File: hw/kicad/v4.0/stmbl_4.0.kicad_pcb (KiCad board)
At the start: 2 copper layers, 100 x 100 mm, 433 parts, among them J1 RJ45_LED, J2 RJ45_LED, J3 RJ45_LED, P1 USB_OTG, P10 CONN_02X06, P11 USB_OTG, P12 CONN_01X04, P13 CONN_01X04, P14 CONN_01X04, P15 CONN_01X02, P2 CONN_01X02, P3 CONN_01X02, P4 CONN_01X02, P5 CONN_01X06, P6 CONN_01X02, P7 CONN_01X04, P8 CONN_01X03, P9 CONN_01X06, Q1 IRLML6344, Q2 IRLML6344, Q3 IRLML6344, Q4 IRLML6344, Q5 IRLML6344, T1 testpoint, T2 testpoint, T44 testpoint, T45 testpoint, T46 testpoint, U1 USBLC6-4SC6, U10 SN65176B, U11 SN65176B, U12 IRAM256a, U13 ACT4088, U14 SN65176B, U15 SN65176B, U16 SN65176B, U17 SN65176B, U18 SN65176B, U19 SN65176B, U2 zldo1117, U20 USBLC6-4SC6, U21 USBLC6-4SC6, U22 USBLC6-4SC6, U23 USBLC6-4SC6, U24 non_plated, U25 STM32F303CBTx, U26 STM32F405VG, U27 ACT4088, U28 ACT4088, U29 USBLC6-4SC6, U3 SI8621, U30 non_plated, U31 non_plated, U32 non_plated, U33 heatsink, U34 fan, U35 non_plated, U36 non_plated, U37 non_plated, U39 non_plated, U4 ACT4088, U5 LNK304D, U6 LM358, U7 LM358, U8 SN65176B, U9 SN65176B, Y1 8M, Y2 8M

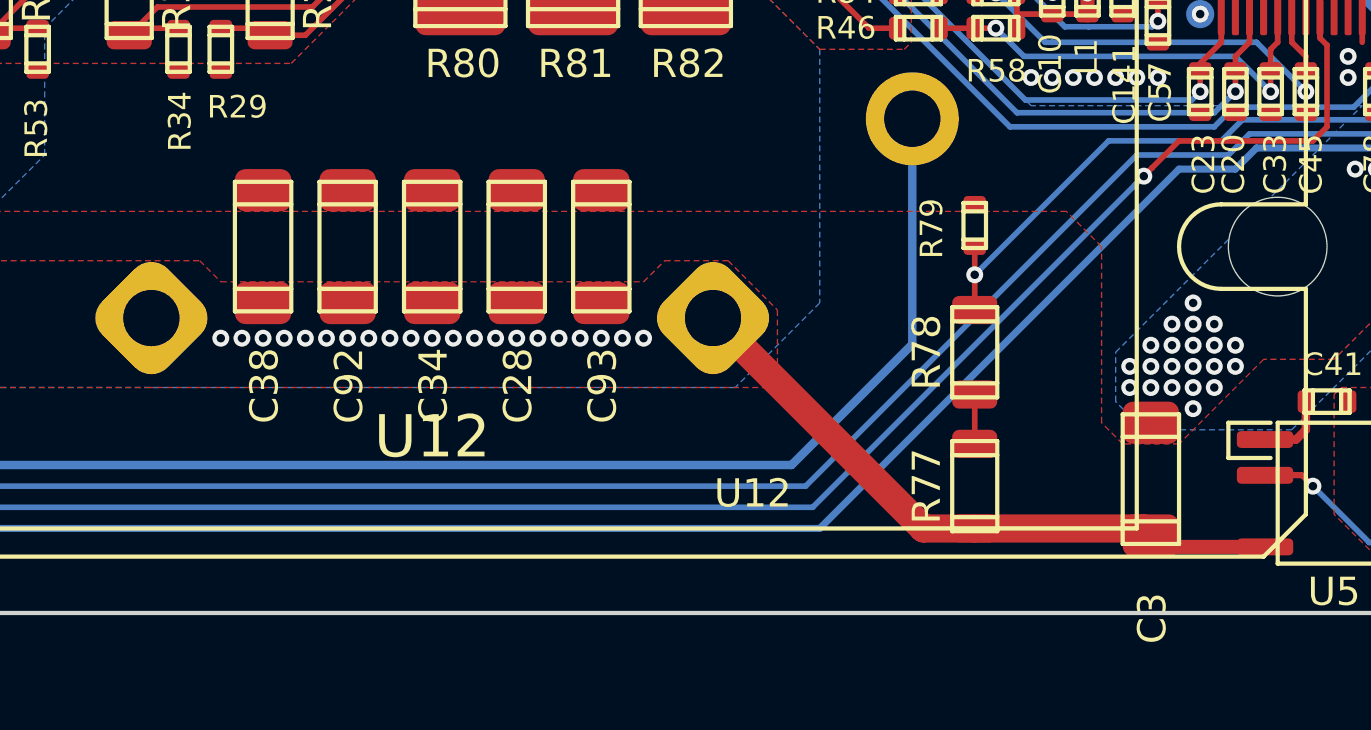
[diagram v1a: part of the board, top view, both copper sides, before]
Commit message: Changed 120uf 1808 to 1210 100uF
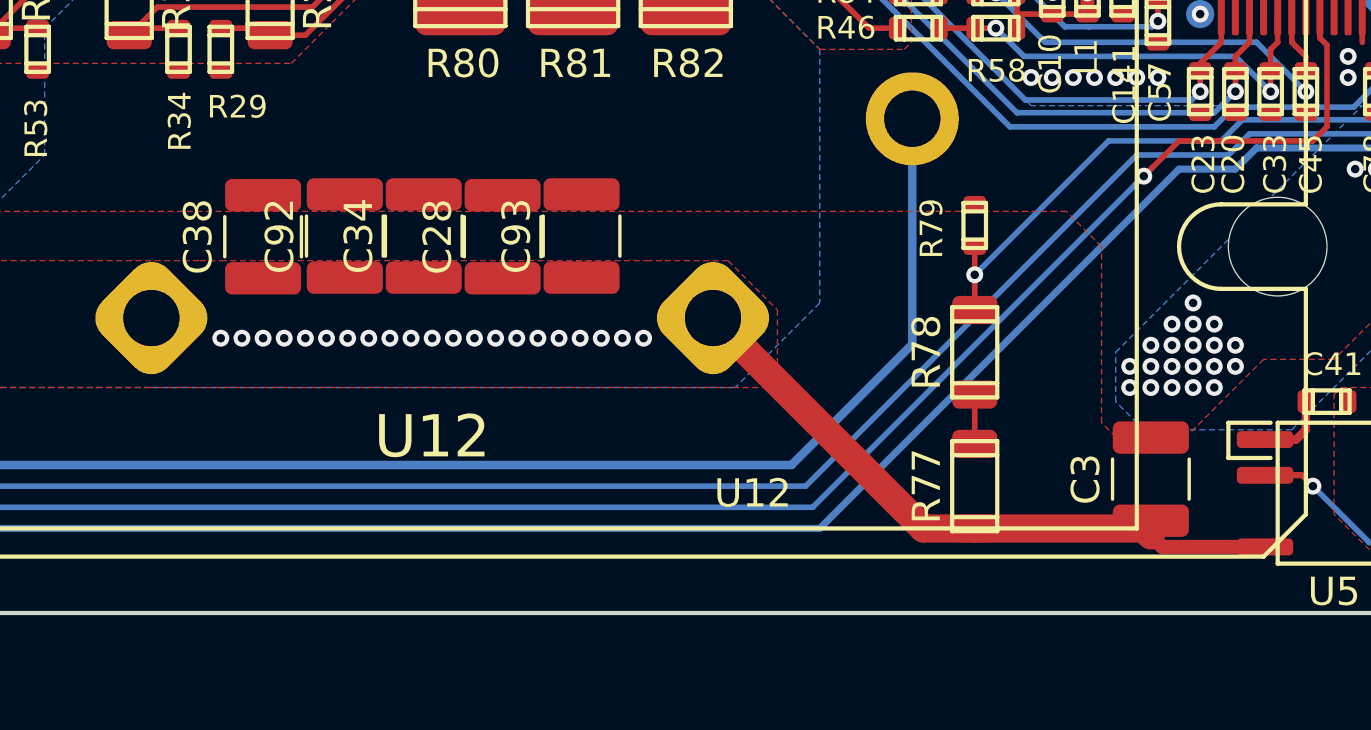
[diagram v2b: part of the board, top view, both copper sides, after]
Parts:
- C28, C3, C34, C38, C92, C93: footprint stmbl:C_1808 -> Capacitor_SMD:C_1210_3225Metric
- moved C93 0.79 mm to (152.3, 136.4)
- moved C28 0.61 mm to (149.5, 136.4)
- moved C34 0.48 mm to (146.7, 136.4)
- moved C92 0.39 mm to (143.9, 136.4)
- moved C38 0.35 mm to (141.0, 136.4)
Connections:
- U7 pad 8: Net-(C37-Pad2) -> (no net)
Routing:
- net GNDPWR: vias 130 -> 129
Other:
- rule pad_to_mask_clearance: 0.1 -> 0

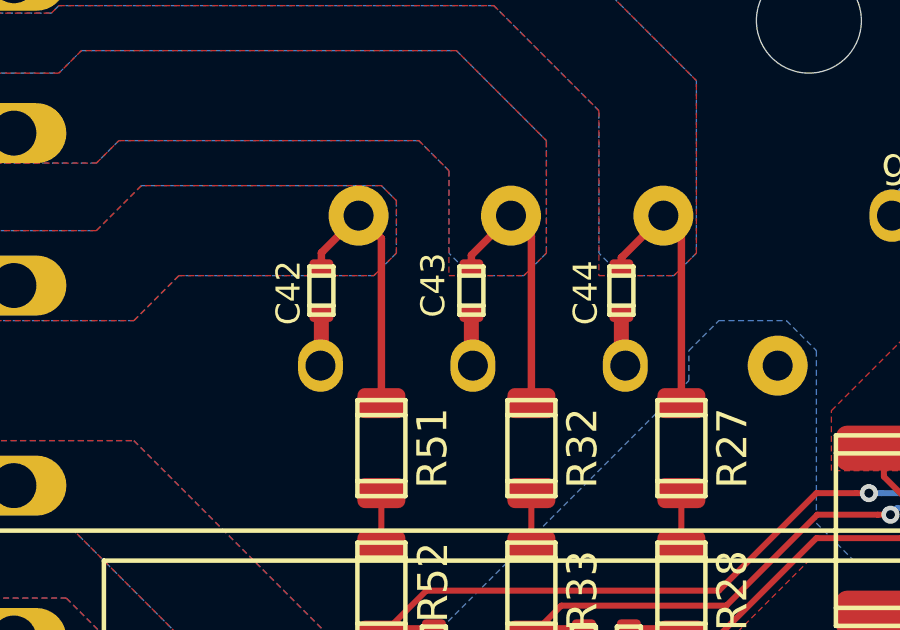
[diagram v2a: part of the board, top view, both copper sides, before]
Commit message: Switch some 2.2uf 0603 to 1uf bypass to get 50V version on jlcpcb
Change 2.2uf 0603 to 0805 on iram to get 50V version on jlcpcb
other cleanup
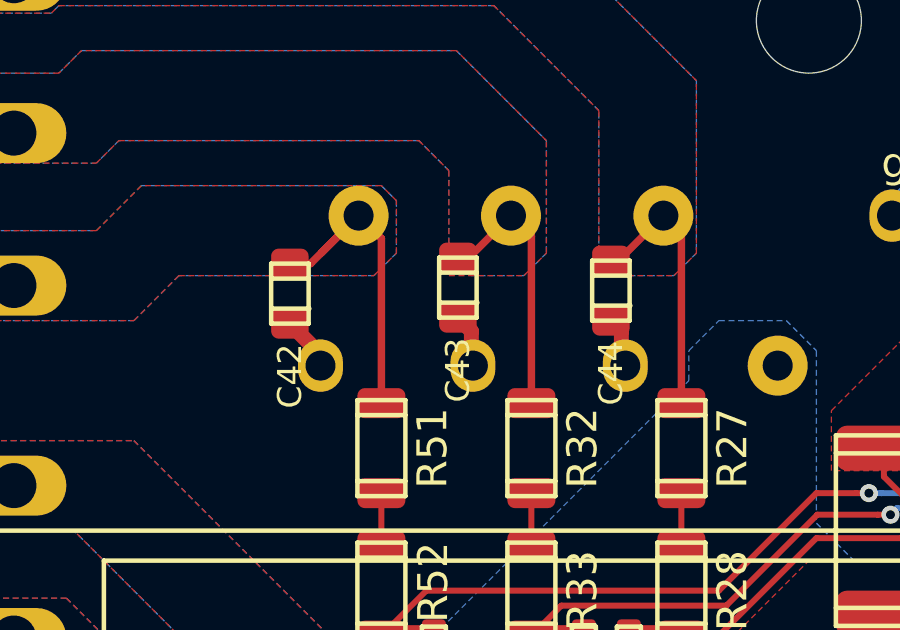
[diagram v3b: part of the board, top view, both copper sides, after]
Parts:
- C101, C102, C129, C133, C134, C135, C136, C137, C139, C140, C141, C142, C144, C18, C50, C62, C65, C8, C88, C90: value 2.2µ -> 2.2u
- C28, C3, C34, C38, C92, C93: value 150n -> 100n
- C42, C43, C44: value 2.2µ -> 2.2u; footprint stmbl:C_0603 -> stmbl:C_0805
- moved C42 1.05 mm to (128.2, 117.8)
- moved C43 0.46 mm to (133.8, 117.7)
- moved C44 0.35 mm to (138.9, 117.8)
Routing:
- net /hv/back-emf/W: track 8.68 -> 11.2 mm

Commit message: couple other PCB changes
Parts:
- moved C93 0.90 mm to (153.2, 136.4)
- moved C38 0.60 mm to (140.4, 136.4)
- moved C28 0.50 mm to (150.0, 136.4)
- moved C92 0.30 mm to (143.6, 136.4)
- moved C34 0.10 mm to (146.8, 136.4)
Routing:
- net VPP: track 22.9 -> 40.1 mm
- net /hv/back-emf/W: track 11.2 -> 8.68 mm
- net +12V: track 140.7 -> 141.8 mm
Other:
- net class Default: via_dia 0.6 -> 0.5
- net class UVW: via_dia 0.6 -> 0.5
- net class UVW_L: via_dia 0.6 -> 0.5
- net class VPP: via_dia 0.6 -> 0.5
- rule via_min_size: 0.6 -> 0.5

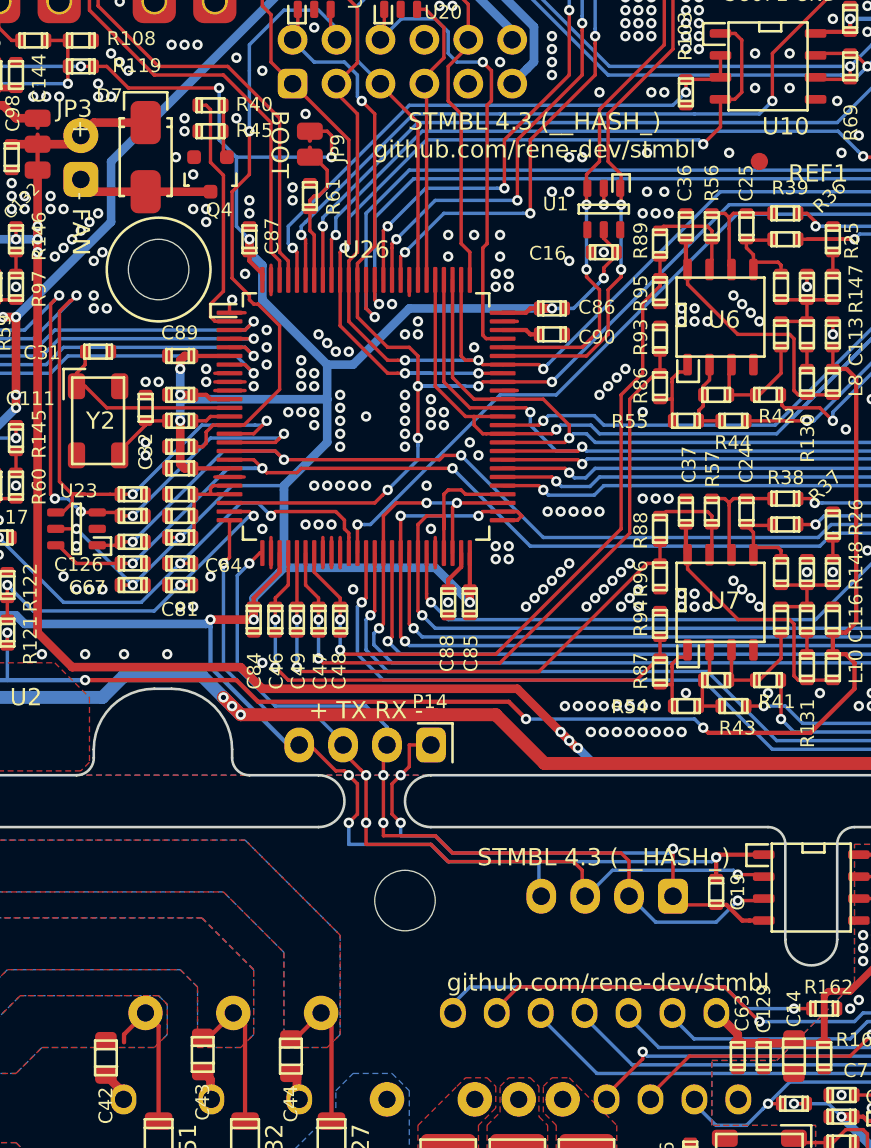
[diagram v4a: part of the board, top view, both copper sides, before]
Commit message: Change Crystals to right footprint
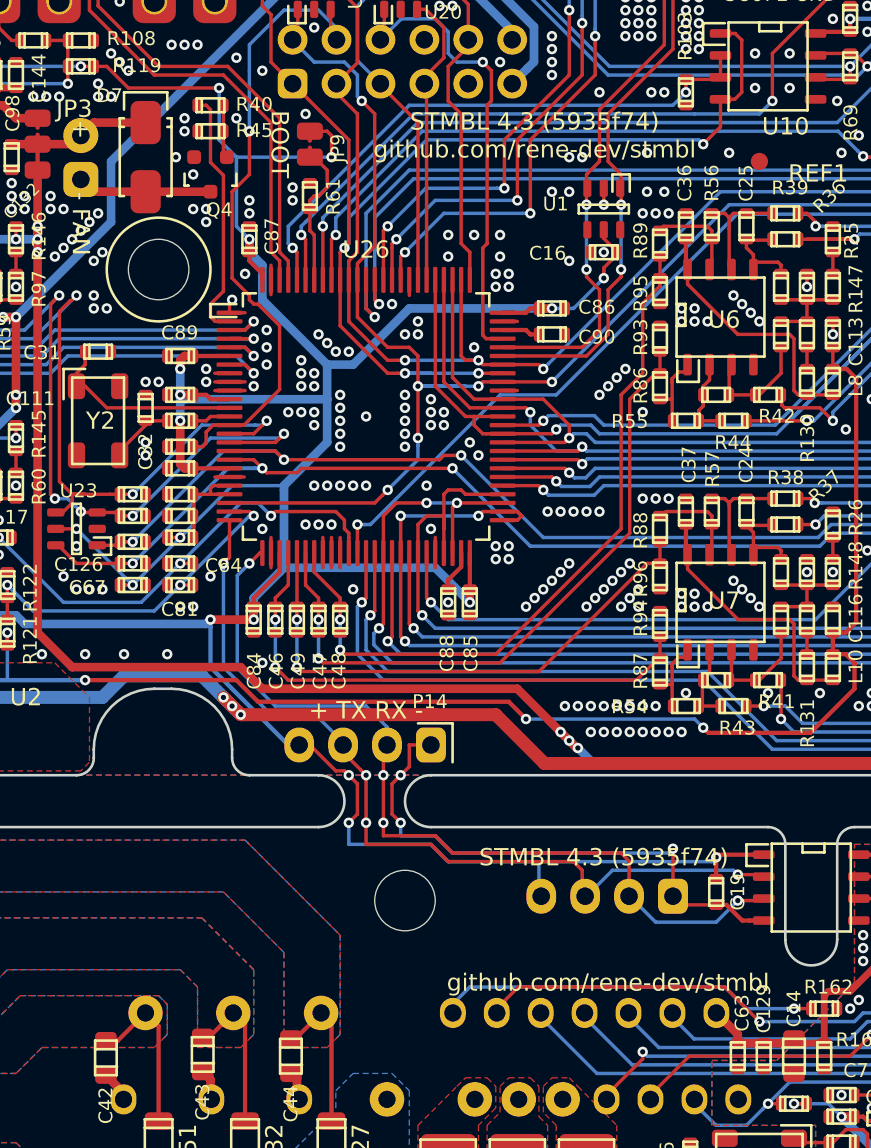
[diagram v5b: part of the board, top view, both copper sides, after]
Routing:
- net /hv/back-emf/W: track 8.68 -> 9.42 mm
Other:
- board text added: "STMBL 4.3 (5935f74)"
- board text added: "STMBL 4.3 (5935f74) github.com/rene-dev/stmbl"
- board text removed: "STMBL 4.3 (__HASH_)"
